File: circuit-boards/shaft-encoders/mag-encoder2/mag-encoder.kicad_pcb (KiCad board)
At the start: 4 copper layers, 21.8 x 27.8 mm, 22 parts, among them J1 CONFIG, J2 0015912055, Q1 BSS84, U1 AP2120N-3.3TRG1, U2 MA732GQ

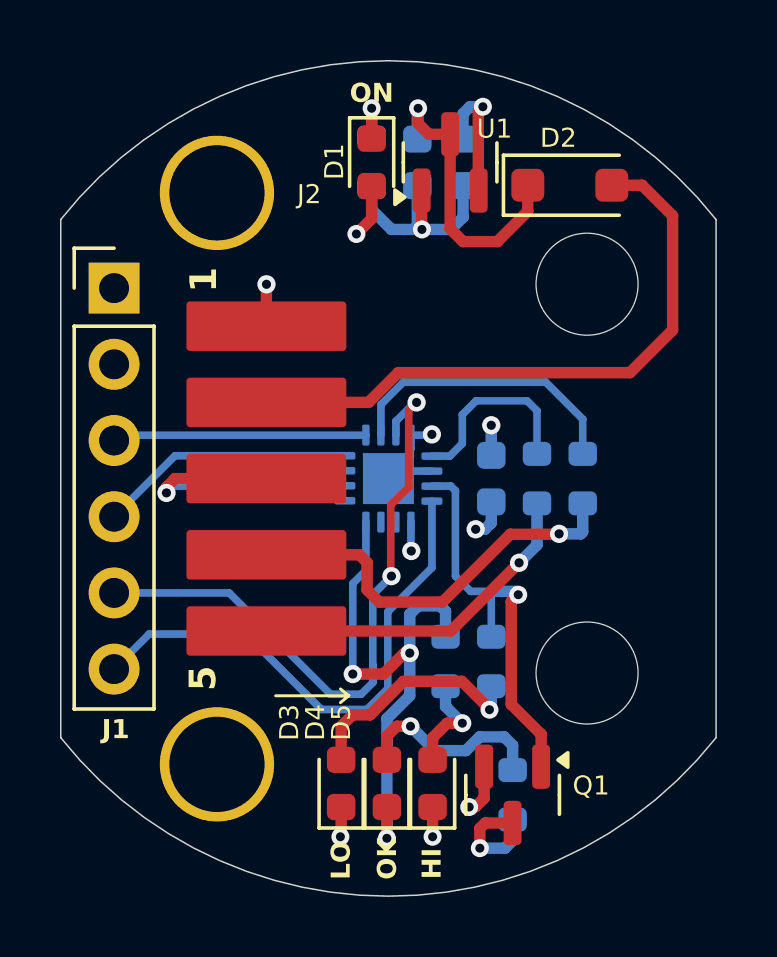
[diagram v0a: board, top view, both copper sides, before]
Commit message: Changed power LED to yellow. Reverse polarity diode to 1N4148
Signed-off-by: Scott <sgberman1@gmail.com>
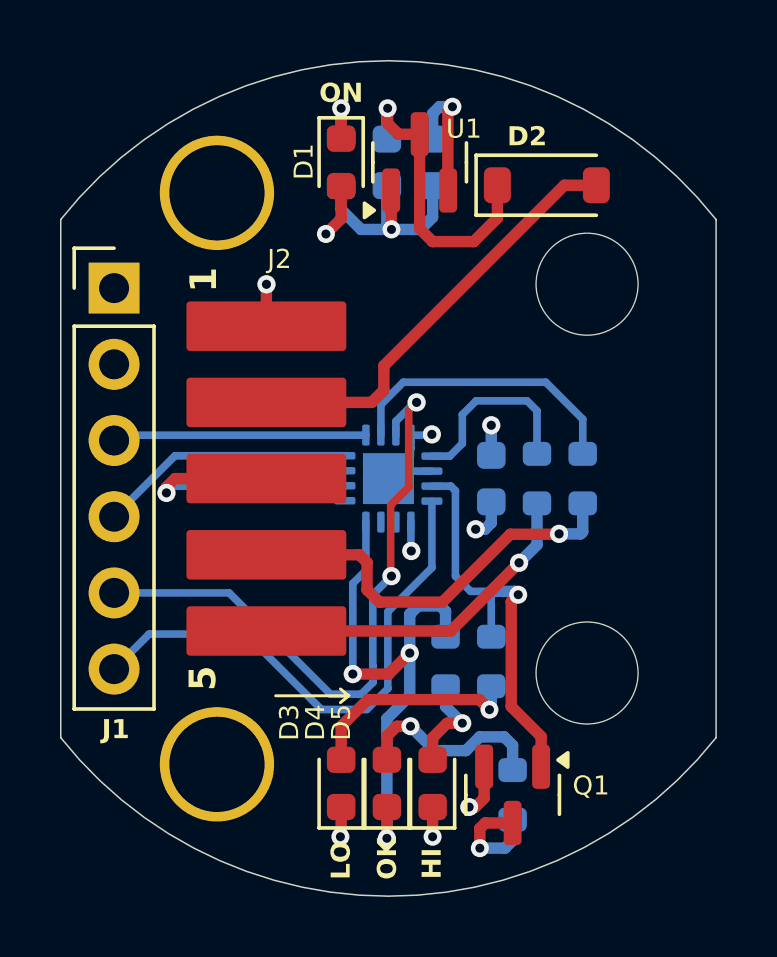
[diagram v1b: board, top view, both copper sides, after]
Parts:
- D2: value NRVB120VLSFT1G -> MMSD4148T1G; footprint Diode_SMD:D_SOD-123F -> Diode_SMD:D_SOD-123
- moved D1 1.02 mm to (229.0, 113.0)
- moved R1 1.02 mm to (229.0, 113.0)
- moved U1 1.02 mm to (231.6, 113.0)
- moved C1 1.02 mm to (232.0, 113.0)
- moved C2 1.02 mm to (230.5, 113.0)
- moved D2 0.76 mm to (235.8, 113.8)
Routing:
- net +5V_IN: track 20.8 -> 14.3 mm
- net Net-(D3-A): track 7.90 -> 7.37 mm
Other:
- board text added: "MAG ENCODER V2"
- board text removed: "MAG ENCODER V1"
